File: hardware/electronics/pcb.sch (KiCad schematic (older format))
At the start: 0 parts

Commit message: Breadboard components added
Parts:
- added B1: ESP32_THING_W_ANT_KEEPOUT, ESP32_THING, symbol ESP32_THING_W_ANT_KEEPOUT
- added C1, C3: 22u, symbol CP
- added C2, C4: 100n, symbol C
- added IC1: 23LC1024, DIL, symbol 23LC1024
- added M1: TSR1-2450, symbol TSR1-2450
- added M2: TSR1-2433, symbol TSR1-2433
- added P1: CONN_01X02, symbol CONN_01X02
- added R1, R2, R3: 10K, symbol R
- added RV1: 10K, symbol POT_TRIM
- added SOM1: Adafruit-Feather-MusicMaker/Amp, symbol Adafruit-Feather-MusicMaker/Amp
- added SW3: SWITCH_PUSHBUTTON, symbol SWITCH_PUSHBUTTON
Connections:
- new net: B1.10 (27), SOM1.22 (XDCS)
- new net: B1.11 (26), SOM1.21 (DREQ)
- new net: B1.32 (0), SW3.P$1
- new net: IC1.7 (~HOLD~/SIO3), R2.2
- new net +12V: M1.1 (+Vin), M2.1 (+Vin), P1.2 (P2)
- new net +3V3: B1.36 (3V3), B1.5 (3V3), C1.1, C2.1, C3.1, C4.1, IC1.8 (VCC), M2.3 (+Vout), R2.1, R3.1, SOM1.2 (3V3)
- new net +5V: M1.3 (+Vout), RV1.3
- new net AUDIO-GROUND: SOM1.B (-SPEAKER_RIGHT), SOM1.D (-SPEAKER_LEFT)
- new net AUDIO-LEFT: SOM1.C (+SPEAKER_LEFT)
- new net AUDIO-RIGHT: SOM1.A (+SPEAKER_RIGHT)
- new net CONTRAST: RV1.2
- new net CONTROL: B1.9 (14), R1.1
- new net D4: B1.33 (4)
- new net D5: B1.31 (2)
- new net D6: B1.30 (15)
- new net D7: B1.29 (5)
- new net EN: B1.34 (17)
- new net GND: B1.1 (GND), B1.21 (GND), B1.37 (GND), B1.4 (GND), B1.40 (GND), C1.2, C2.2, C3.2, C4.2, IC1.4 (VSS), M1.2 (GND), M2.2 (GND), P1.1 (P1), R1.2, RV1.1, SOM1.4 (GND), SW3.P$2
- new net RS: B1.35 (16)
- new net SPI-MISO: B1.26 (19), IC1.2 (SO/SIO1), SOM1.13 (MISO)
- new net SPI-MOSI: B1.27 (23), IC1.5 (SI/SIO0), SOM1.12 (MOSI)
- new net SPI-RAM-CS: B1.25 (22), IC1.1 (~CS)
- new net SPI-SCK: B1.28 (18), SOM1.11 (SCK)
- new net SPI-XCS: B1.12 (25), SOM1.20 (MP3CS)
- no-connect marks 0 -> 21
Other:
- note added: "BUFFER"
- note added: "CHECK THIS!"
- note added: "In final version need to have two 3.3V \nsupplies for digital (DVDD) and analog \npower for the VS1053 (AVDD)."
- note added: "LCD"
- note added: "PINS HAVE CHANGED!!!"
- note added: "POWER"
- note added: "TEMPORARY FOR BREADBOARD.\nNEEDS TO BE EXPANDED WITH \nVS1053 CIRCUIT."

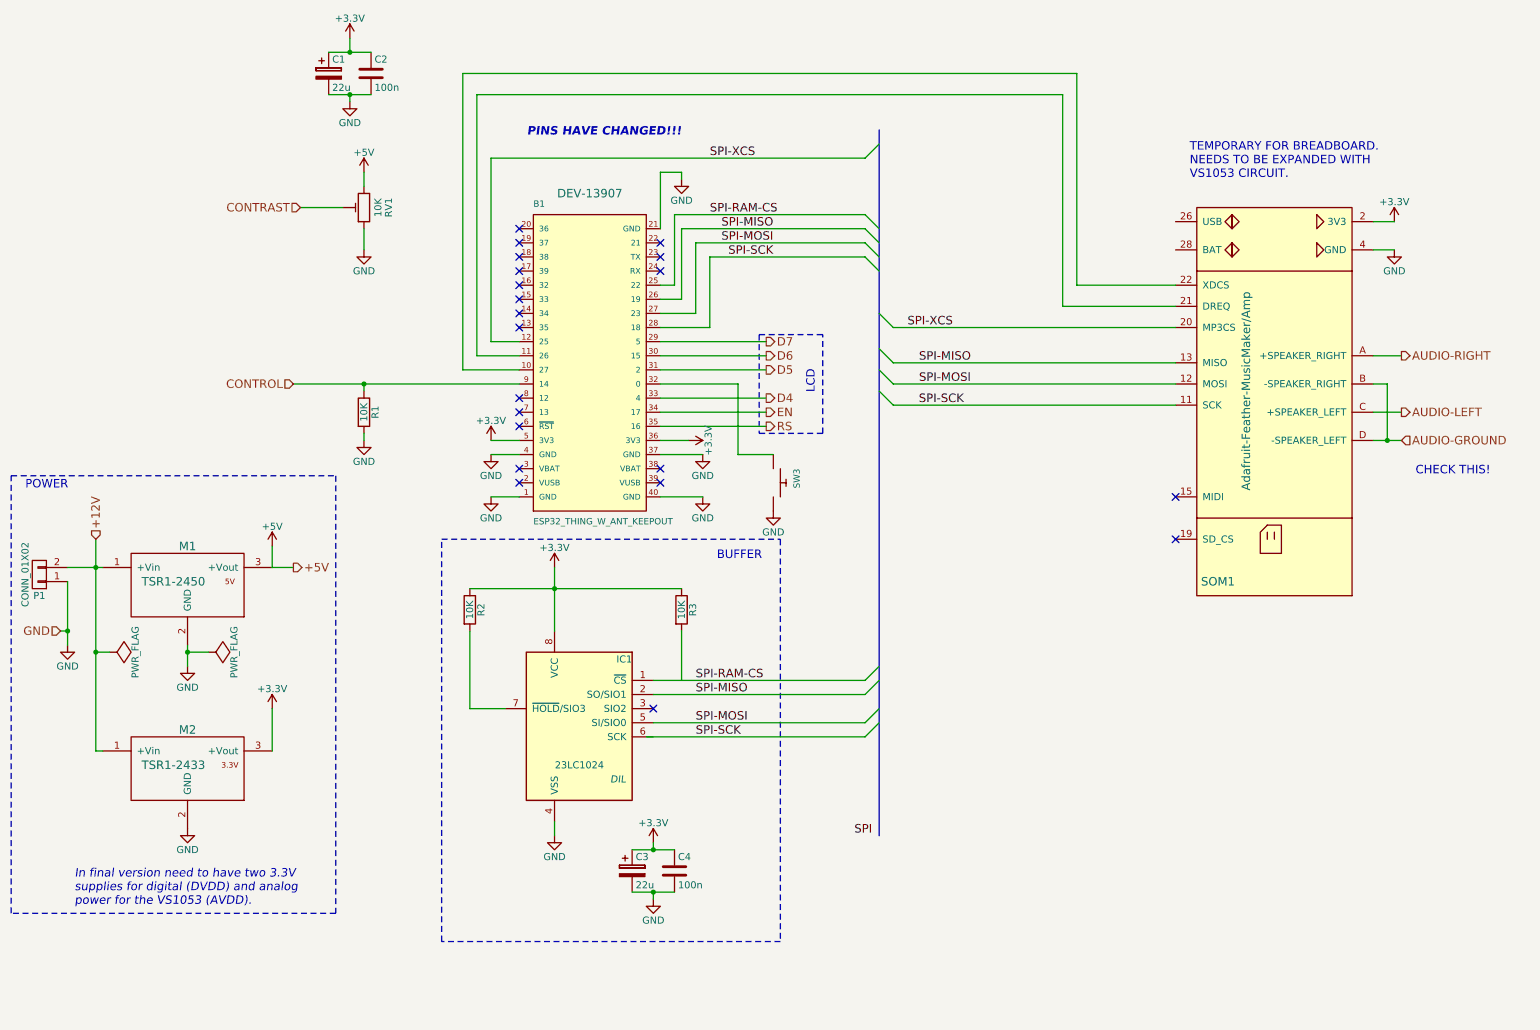
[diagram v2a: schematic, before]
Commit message: Added level shifting buffers
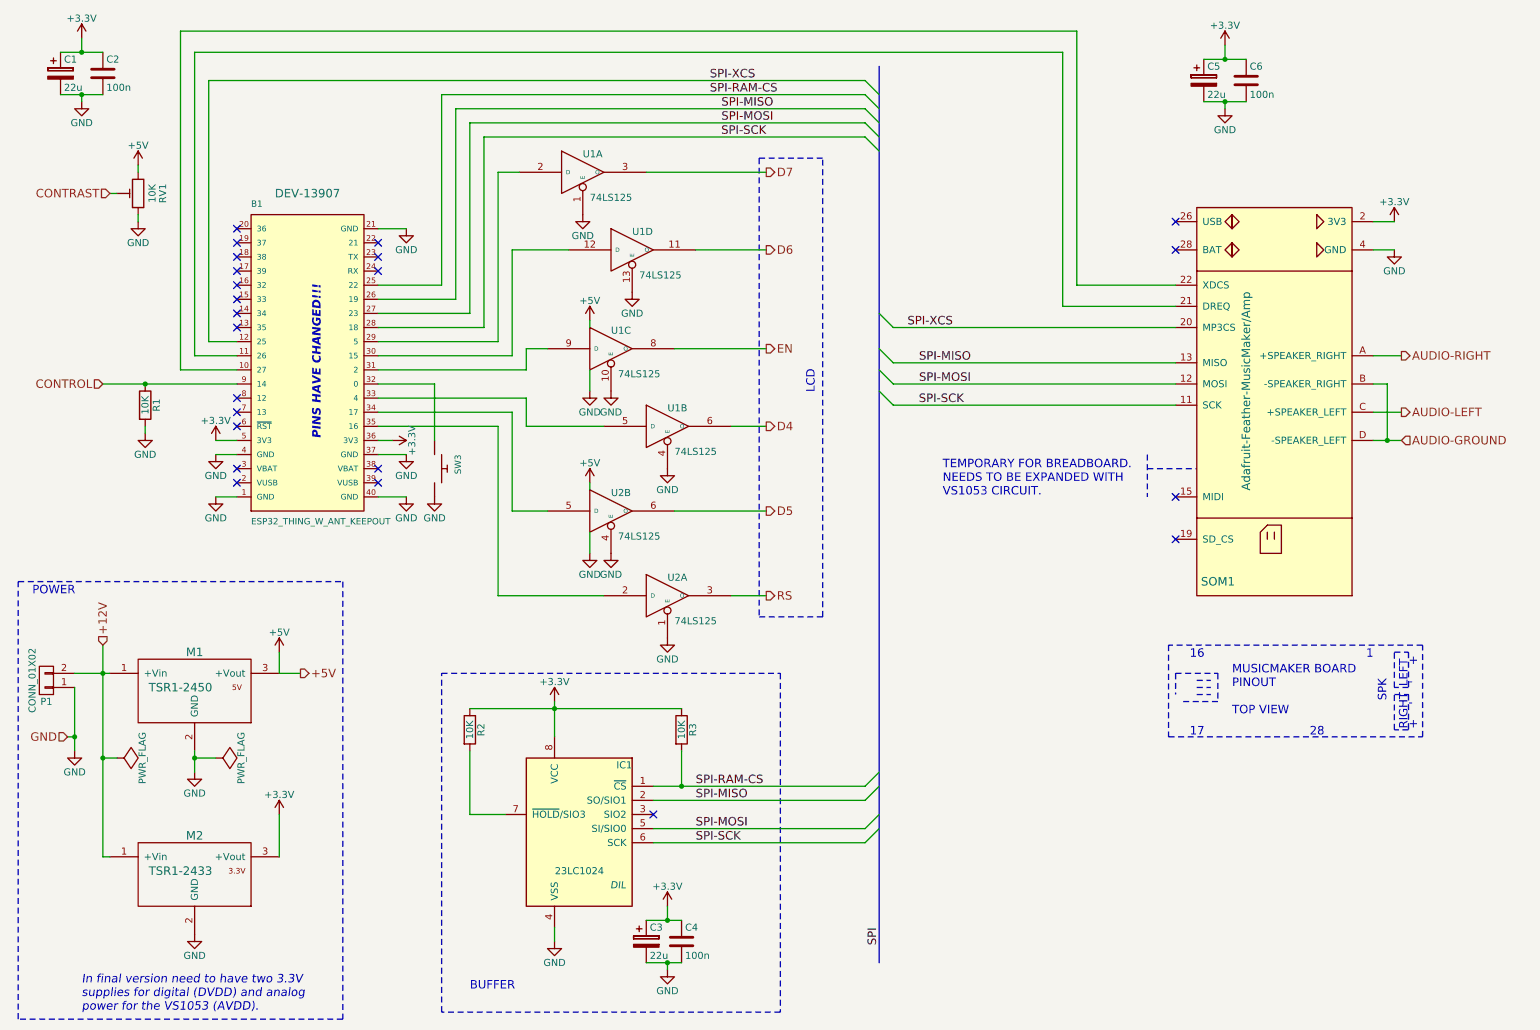
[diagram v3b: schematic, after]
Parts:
- added C5: 22u, symbol CP
- added C6: 100n, symbol C
- added U1, U2: 74LS125, symbol 74LS125
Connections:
- net +3V3: now also C5.1, C6.1
- net +5V: now also U1.14 (VCC), U1.14 (VCC), U1.14 (VCC), U1.14 (VCC), U2.14 (VCC), U2.14 (VCC)
- net D4: now also U1.6 (O); no longer B1.33 (4)
- net D5: now also U2.6 (O); no longer B1.31 (2)
- net D6: now also U1.11 (O); no longer B1.30 (15)
- net D7: now also U1.3 (O); no longer B1.29 (5)
- net EN: now also U1.8 (O); no longer B1.34 (17)
- net GND: now also C5.2, C6.2, U1.1 (E), U1.10 (E), U1.13 (E), U1.4 (E), U1.7 (GND), U1.7 (GND), U1.7 (GND), U1.7 (GND), U2.1 (E), U2.4 (E), U2.7 (GND), U2.7 (GND)
- net RS: now also U2.3 (O); no longer B1.35 (16)
- net SPI-RAM-CS: now also R3.2
- net SPI-SCK: now also IC1.6 (SCK)
- new net: B1.29 (5), U1.2 (D)
- new net: B1.30 (15), U1.12 (D)
- new net: B1.31 (2), U1.9 (D)
- new net: B1.33 (4), U1.5 (D)
- new net: B1.34 (17), U2.5 (D)
- new net: B1.35 (16), U2.2 (D)
- no-connect marks 21 -> 23
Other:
- note added: "+"
- note added: "-"
- note added: "1"
- note added: "16"
- note added: "17\n"
- note added: "28"
- note added: "LEFT"
- note added: "MUSICMAKER BOARD \nPINOUT\n\nTOP VIEW"
- note added: "RIGHT"
- note added: "SPK"
- note removed: "CHECK THIS!"
- moved on the sheet: B1, C1, C2, C3, C4, IC1, M1, M2, P1, R1, R2, R3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

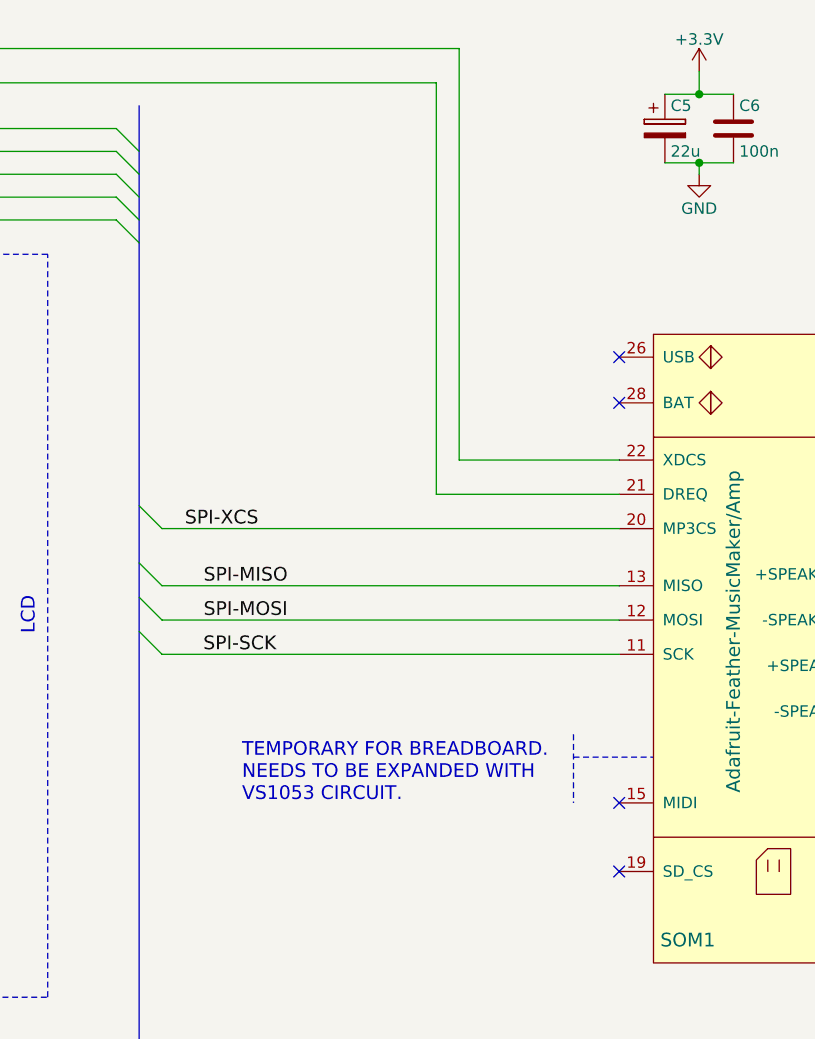
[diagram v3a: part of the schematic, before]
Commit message: Added test-rig project
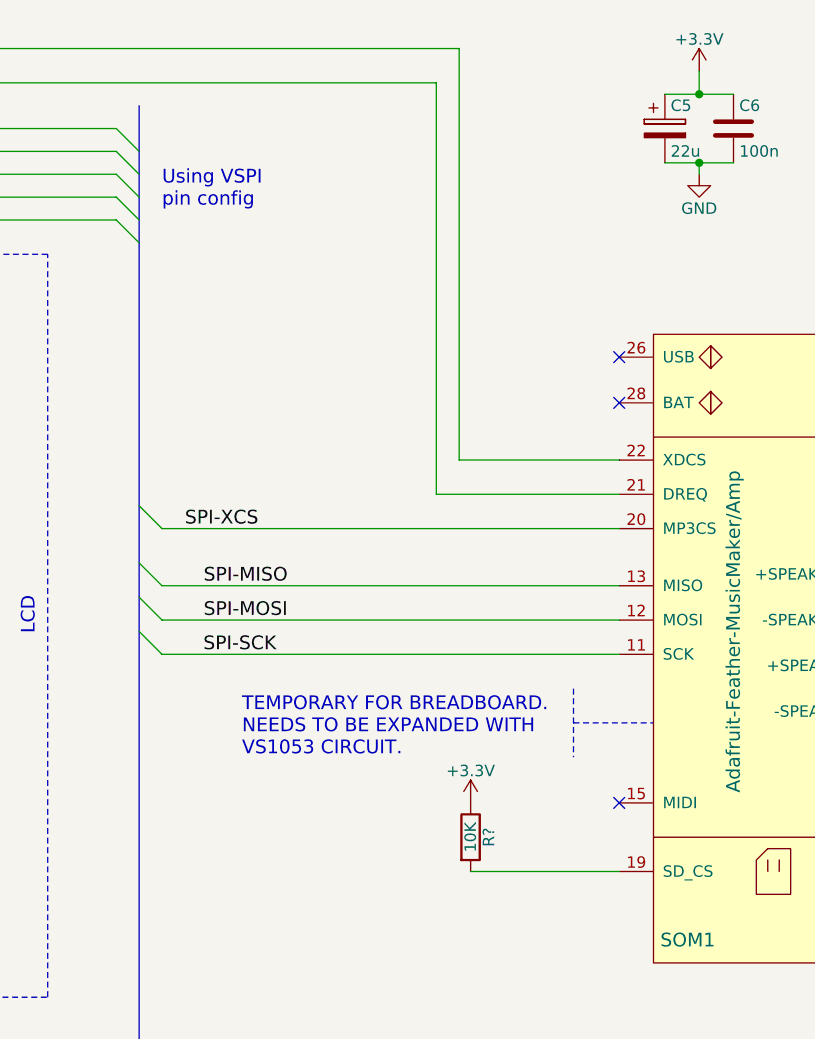
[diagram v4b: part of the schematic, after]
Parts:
- added R?: 10K, symbol R
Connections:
- net +3V3: now also R?.1
- net at SOM1.19 (SD_CS): now also R?.2
- no-connect marks 23 -> 22
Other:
- note added: "Using VSPI \npin config"
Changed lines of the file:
@@
 Wire Wire Line
 	1750 3100 2150 3100
-Text Notes 7150 4000 0    60   ~ 0
+Text Notes 7150 3800 0    60   ~ 0
 TEMPORARY FOR BREADBOARD.\nNEEDS TO BE EXPANDED WITH \nVS1053 CIRCUIT.
 $Comp
@@
 $EndComp
 NoConn ~ 8800 4000
-NoConn ~ 8800 4300
 Wire Wire Line
 	2450 5250 2600 5250
@@
 $EndComp
 Wire Notes Line
-	8600 3700 8600 4000
-Wire Notes Line
-	8600 3800 8950 3800
+	8600 3500 8600 3800
+Wire Notes Line
+	8600 3650 8950 3650
 Wire Wire Line
 	6600 6450 5100 6450
@@
 	5300 5800 5300 6050
 Connection ~ 5300 6050
+$Comp
+L R R?
+U 1 1 5D52F7DB
+P 8150 4150
+F 0 "R?" V 8230 4150 50  0000 C CNN
+F 1 "10K" V 8150 4150 50  0000 C CNN
+F 2 "" V 8080 4150 50  0000 C CNN
+F 3 "" H 8150 4150 50  0000 C CNN
+	1    8150 4150
+	1    0    0    -1
+$EndComp
+Wire Wire Line
+	8800 4300 8150 4300
+$Comp
+L +3.3V #PWR?
+U 1 1 5D52FFC9
+P 8150 4000
+F 0 "#PWR?" H 8150 3850 50  0001 C CNN
+F 1 "+3.3V" H 8150 4140 50  0000 C CNN
+F 2 "" H 8150 4000 50  0000 C CNN
+F 3 "" H 8150 4000 50  0000 C CNN
+	1    8150 4000
+	1    0    0    -1
+$EndComp
+Text Notes 6800 1400 0    60   ~ 0
+Using VSPI \npin config
 $EndSCHEMATC
